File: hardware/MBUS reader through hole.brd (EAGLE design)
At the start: 20.8 x 72.6 mm, 18 parts, among them Q1 BC337, Q2 BC337, T1 BC307

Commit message: modified files
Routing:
- net GND: track 79.1 -> 60.3 mm
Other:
- board text added: "Designed in"
- board text added: "North Wales"
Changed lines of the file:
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@@
 <wire x1="75.7928" y1="7.258" x2="96.4448" y2="7.258" width="0" layer="20"/>
 <wire x1="3" y1="79.9" x2="3" y2="79.4" width="0" layer="121"/>
-<text x="80.914" y="62.7056" size="0.762" layer="121" font="vector" ratio="20" rot="R90">www.openenergymonitor.org</text>
-<text x="82.1692" y="78.1948" size="0.7112" layer="121" font="vector" ratio="20" rot="R270">Designed in North Wales
+<text x="80.914" y="62.7056" size="0.762" layer="21" font="vector" ratio="20" rot="R90">www.openenergymonitor.org</text>
+<text x="82.1692" y="78.1948" size="0.7112" layer="21" font="vector" ratio="20" rot="R270">Designed in North Wales
 by Trystan Lea,
 Glyn Hudson, John Cantor
 and Shiromini Satkunarajah
 </text>
-<text x="81.400640625" y="31.442121875" size="0.7112" layer="21" font="vector" ratio="15" rot="SR0">Made in UK</text>
 <rectangle x1="82.372440625" y1="33.122321875" x2="82.378740625" y2="33.128721875" layer="21"/>
 <rectangle x1="82.366040625" y1="33.128721875" x2="82.378740625" y2="33.135021875" layer="21"/>
@@
 <text x="91.900640625" y="70.742121875" size="0.7112" layer="21" font="vector" ratio="15" rot="SR270">OUT+</text>
 <text x="79.250640625" y="70.192121875" size="0.7112" layer="21" font="vector" ratio="15" rot="SR270">OUT-</text>
+<text x="81.400640625" y="32.342121875" size="0.7112" layer="21" font="vector" ratio="15" rot="SR0">North Wales</text>
+<text x="81.600640625" y="36.942121875" size="0.7112" layer="21" font="vector" ratio="15" rot="SR0">Designed in </text>
+<text x="81.400640625" y="31.292121875" size="0.7112" layer="21" font="vector" ratio="15" rot="SR0">Made in UK</text>
 </plain>
 <attributes>
@@
 <elements>
 <element name="Q1" library="transistor" package="TO92" value="BC337" x="93.1952" y="54.0428" smashed="yes">
-<attribute name="VALUE" x="90.2208" y="52.7304" size="0.8128" layer="27" font="vector" ratio="20" rot="R90"/>
+<attribute name="VALUE" x="90.2208" y="52.7304" size="0.8128" layer="21" font="vector" ratio="20" rot="R90"/>
 </element>
 <element name="Q2" library="transistor" package="TO92" value="BC337" x="93.1952" y="58.5856" smashed="yes">
-<attribute name="VALUE" x="90.2208" y="56.9976" size="0.8128" layer="27" font="vector" ratio="20" rot="R90"/>
+<attribute name="VALUE" x="90.2208" y="56.9976" size="0.8128" layer="21" font="vector" ratio="20" rot="R90"/>
 </element>
 <element name="T1" library="transistor-pnp" package="TO92" value="BC307" x="93.1952" y="64.8904" smashed="yes" rot="R180">
-<attribute name="VALUE" x="90.269" y="63.3796" size="0.8128" layer="27" font="vector" ratio="20" rot="R90"/>
+<attribute name="VALUE" x="90.269" y="63.3796" size="0.8128" layer="21" font="vector" ratio="20" rot="R90"/>
 </element>
 <element name="R3" library="resistor" package="0204/7" value="39k" x="84" y="55" smashed="yes" rot="R180">
 <attribute name="NAME" x="83.3956" y="55.3212" size="0.8128" layer="25" font="vector" ratio="20" rot="R180"/>
-<attribute name="VALUE" x="86.3012" y="55.4736" size="0.8128" layer="27" font="vector" ratio="20" rot="R180"/>
+<attribute name="VALUE" x="86.3012" y="55.4736" size="0.8128" layer="21" font="vector" ratio="20" rot="R180"/>
 </element>
 <element name="R2" library="resistor" package="0204/7" value="33k" x="84.005" y="57.615" smashed="yes" rot="R180">
 <attribute name="NAME" x="83.2456" y="57.862" size="0.8128" layer="25" font="vector" ratio="20" rot="R180"/>
-<attribute name="VALUE" x="86.4488" y="57.9644" size="0.8128" layer="27" font="vector" ratio="20" rot="R180"/>
+<attribute name="VALUE" x="86.4488" y="57.9644" size="0.8128" layer="21" font="vector" ratio="20" rot="R180"/>
 </element>
 <element name="R6" library="resistor" package="0204/7" value="22k" x="82.575" y="45.755" smashed="yes" rot="R90">
@@
 <element name="R1" library="resistor" package="0204/7" value="220k" x="84.005" y="60.155" smashed="yes" rot="R180">
 <attribute name="NAME" x="83.1956" y="60.5028" size="0.8128" layer="25" font="vector" ratio="20" rot="R180"/>
-<attribute name="VALUE" x="86.4012" y="60.4552" size="0.8128" layer="27" font="vector" ratio="20" rot="R180"/>
+<attribute name="VALUE" x="86.4012" y="60.4552" size="0.8128" layer="21" font="vector" ratio="20" rot="R180"/>
 </element>
 <element name="R4" library="resistor" package="0204/7" value="1k" x="84.005" y="52.535" smashed="yes" rot="R180">
 <attribute name="NAME" x="83.2956" y="52.7828" size="0.8128" layer="25" font="vector" ratio="20" rot="R180"/>
-<attribute name="VALUE" x="85.8012" y="52.8828" size="0.8128" layer="27" font="vector" ratio="20" rot="R180"/>
+<attribute name="VALUE" x="85.8012" y="52.8828" size="0.8128" layer="21" font="vector" ratio="20" rot="R180"/>
 </element>
 <element name="R5" library="resistor" package="0204/7" value="1k" x="80.035" y="45.755" smashed="yes" rot="R270">
@@
 <wire x1="94.4652" y1="58.5856" x2="94.4652" y2="60.80113125" width="0.4064" layer="16"/>
 <wire x1="94.4652" y1="60.80113125" x2="93.65813125" y2="61.6082" width="0.4064" layer="16"/>
-<wire x1="86.7934" y1="24.2808" x2="83.8126" y2="21.3" width="0.4064" layer="1"/>
-<wire x1="83.8126" y1="21.3" x2="79.15" y2="21.3" width="0.4064" layer="1"/>
-<wire x1="79.15" y1="21.3" x2="77.5" y2="22.95" width="0.4064" layer="1"/>
-<wire x1="77.5" y1="22.95" x2="77.5" y2="30.5" width="0.4064" layer="1"/>
 </signal>
 <signal name="D5">
@@
 <wire x1="93.1952" y1="60.4906" x2="93.1952" y2="57.4564875" width="0.4064" layer="16"/>
 <wire x1="93.1952" y1="57.4564875" x2="90.8584" y2="55.1196875" width="0.4064" layer="16"/>
-<wire x1="90.8584" y1="55.1196875" x2="90.8584" y2="53.2156" width="0.4064" layer="16"/>
-<wire x1="90.8584" y1="53.2156" x2="87.655" y2="50.0122" width="0.4064" layer="16"/>
+<wire x1="90.8584" y1="55.1196875" x2="90.8584" y2="53.1156" width="0.4064" layer="16"/>
+<wire x1="90.8584" y1="53.1156" x2="87.655" y2="50.0122" width="0.4064" layer="16"/>
 <wire x1="94.4652" y1="64.8904" x2="94.4652" y2="61.7606" width="0.4064" layer="1"/>
 <wire x1="94.4652" y1="61.7606" x2="93.1952" y2="60.4906" width="0.4064" layer="1"/>
@@
 <wire x1="93.1952" y1="55.9478" x2="93.1164" y2="55.869" width="0.4064" layer="1"/>
 <wire x1="93.1164" y1="55.869" x2="93.1164" y2="53.4924" width="0.4064" layer="1"/>
-<wire x1="93.1164" y1="53.4924" x2="92.159" y2="52.535" width="0.4064" layer="1"/>
-<wire x1="92.159" y1="52.535" x2="87.815" y2="52.535" width="0.4064" layer="1"/>
+<wire x1="93.1164" y1="53.4924" x2="91.859" y2="52.535" width="0.4064" layer="1"/>
+<wire x1="91.859" y1="52.535" x2="87.815" y2="52.535" width="0.4064" layer="1"/>
 </signal>
 <signal name="24V">

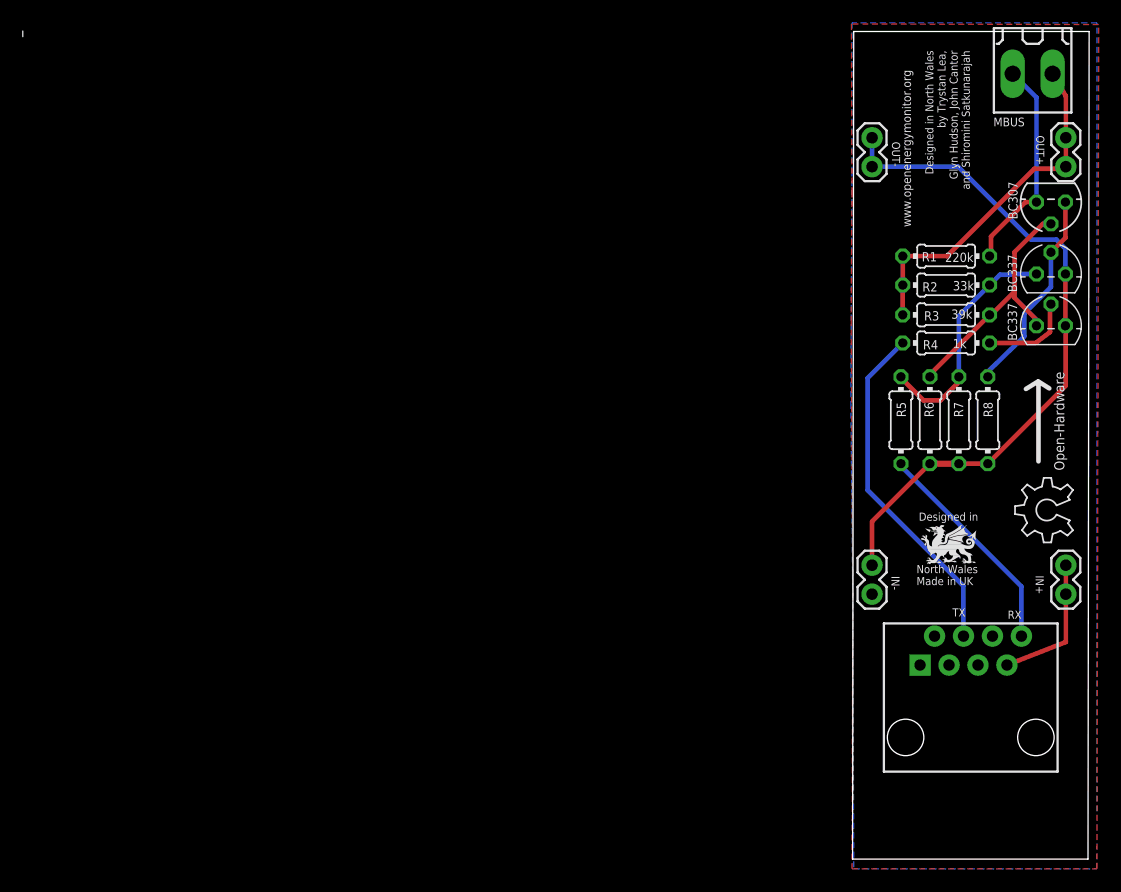
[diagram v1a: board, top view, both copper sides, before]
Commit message: through hole with connector blocks
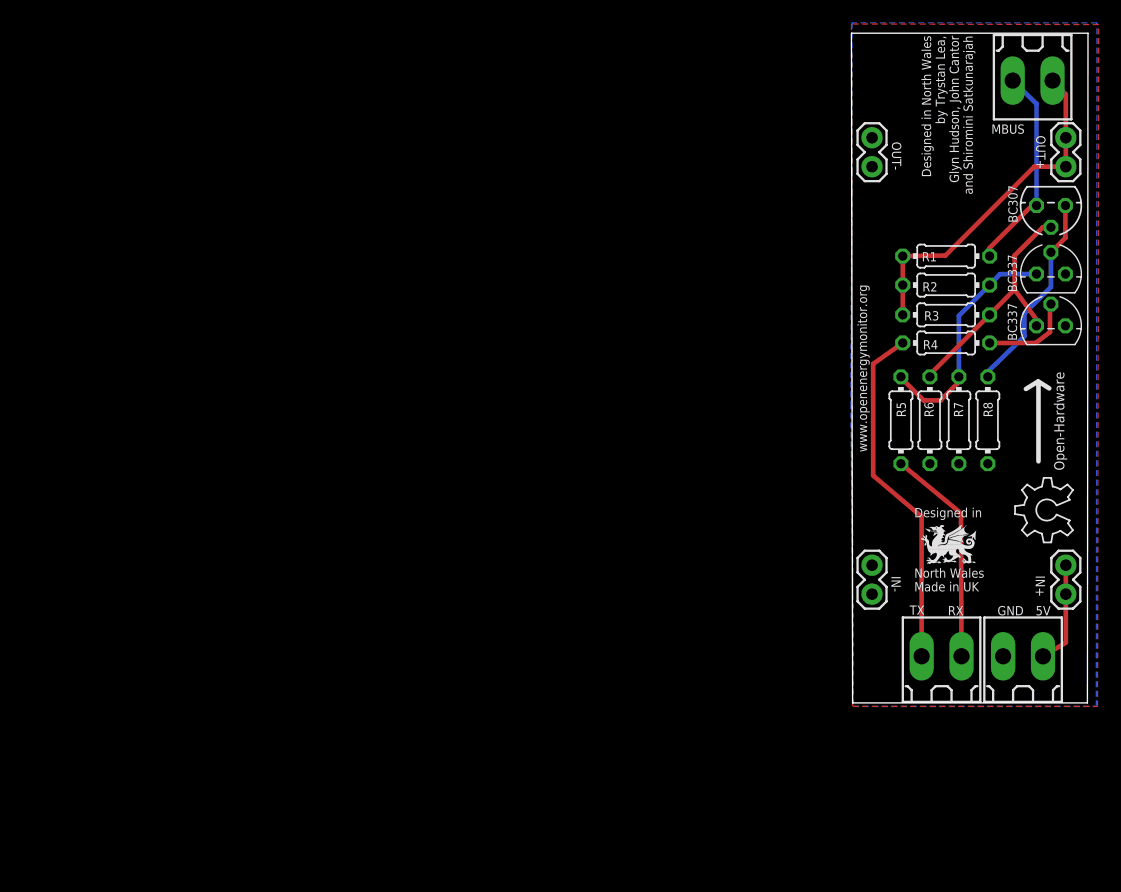
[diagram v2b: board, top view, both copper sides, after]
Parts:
- removed U$13: RJ45-8PTH, SparkFun-Connectors:RJ45-8
- added MBUS1, MBUS2: (no value), con-weidmueller-sl35:180-2
- moved MBUS 0.60 mm to (91.6, 75.6)
- moved T1 0.30 mm to (93.2, 64.6)
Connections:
- net 5V: now also MBUS2.2; no longer U$13.7
- net A6: now also MBUS1.2; no longer U$13.8
- net D5: now also MBUS1.1; no longer U$13.4
- net GND: now also MBUS2.1; no longer U$13.5
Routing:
- net GND: track 60.3 -> 0.04 mm
- net 5V: track 12.3 -> 9.12 mm
- net N$1: track 19.2 -> 18.5 mm
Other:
- board size 20.8 x 72.6 mm -> 20.8 x 58.8 mm
- board text added: "5V"
- board text added: "GND"

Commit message: neater
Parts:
- moved MBUS 5.30 mm to (86.3, 75.6)
- moved MBUS2 1.02 mm to (89.7, 25.1)
- moved MBUS1 1.02 mm to (82.6, 25.1)
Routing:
- net 24V: track 30.7 -> 35.1 mm
- net N$1: track 18.5 -> 20.4 mm
- net A6: track 19.4 -> 18.5 mm
- net 5V: track 9.12 -> 9.94 mm
- net D5: track 31.1 -> 30.3 mm
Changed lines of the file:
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@@
 <setting verticaltext="up"/>
 </settings>
-<grid distance="1.96850394" unitdist="mil" unit="mil" style="lines" multiple="1" display="yes" altdistance="0.635" altunitdist="mm" altunit="mm"/>
+<grid distance="10" unitdist="mil" unit="mil" style="lines" multiple="1" display="yes" altdistance="0.635" altunitdist="mm" altunit="mm"/>
 <layers>
 <layer number="1" name="Top" color="4" fill="1" visible="yes" active="yes"/>
@@
 <wire x1="75.7928" y1="20.958" x2="96.3948" y2="20.958" width="0" layer="20"/>
 <text x="77.064" y="42.9556" size="0.8128" layer="21" font="vector" ratio="20" rot="R90">www.openenergymonitor.org</text>
-<text x="81.8692" y="79.4948" size="0.8128" layer="21" font="vector" ratio="20" rot="R270">Designed in North Wales
+<text x="88.2192" y="60.6988" size="0.8128" layer="21" font="vector" ratio="20" rot="MR270">Designed in North Wales
 by Trystan Lea,
 Glyn Hudson, John Cantor
@@
 </element>
 <element name="LOGO1" library="ohw-logo" package="OSHW_6X200_NOTEXT" value="OSHW_LOGO_6MILX0200-NT" x="95.1238" y="35.0372" rot="R90"/>
-<element name="MBUS" library="con-weidmueller-sl35" library_urn="urn:adsk.eagle:library:199" package="180-2" value="" x="91.5876" y="75.5524" smashed="yes" rot="R180">
-<attribute name="MF" value="" x="91.5876" y="75.5524" size="1.778" layer="27" rot="R180" display="off"/>
-<attribute name="MPN" value="" x="91.5876" y="75.5524" size="1.778" layer="27" rot="R180" display="off"/>
-<attribute name="NAME" x="90.8876" y="71.7024" size="0.8128" layer="25" rot="R180"/>
-<attribute name="OC_FARNELL" value="unknown" x="91.5876" y="75.5524" size="1.778" layer="27" rot="R180" display="off"/>
-<attribute name="OC_NEWARK" value="unknown" x="91.5876" y="75.5524" size="1.778" layer="27" rot="R180" display="off"/>
-<attribute name="VALUE" x="93.3376" y="73.8024" size="1.27" layer="27" rot="R180"/>
+<element name="MBUS" library="con-weidmueller-sl35" library_urn="urn:adsk.eagle:library:199" package="180-2" value="" x="86.2876" y="75.5524" smashed="yes" rot="R180">
+<attribute name="MF" value="" x="86.2876" y="75.5524" size="1.778" layer="27" rot="R180" display="off"/>
+<attribute name="MPN" value="" x="86.2876" y="75.5524" size="1.778" layer="27" rot="R180" display="off"/>
+<attribute name="NAME" x="85.5876" y="71.7024" size="0.8128" layer="25" rot="R180"/>
+<attribute name="OC_FARNELL" value="unknown" x="86.2876" y="75.5524" size="1.778" layer="27" rot="R180" display="off"/>
+<attribute name="OC_NEWARK" value="unknown" x="86.2876" y="75.5524" size="1.778" layer="27" rot="R180" display="off"/>
+<attribute name="VALUE" x="88.0376" y="73.8024" size="1.27" layer="27" rot="R180"/>
 </element>
-<element name="MBUS1" library="con-weidmueller-sl35" library_urn="urn:adsk.eagle:library:199" package="180-2" value="" x="83.6" y="25.05" smashed="yes">
-<attribute name="MF" value="" x="83.6" y="25.05" size="1.778" layer="27" display="off"/>
-<attribute name="MPN" value="" x="83.6" y="25.05" size="1.778" layer="27" display="off"/>
-<attribute name="OC_FARNELL" value="unknown" x="83.6" y="25.05" size="1.778" layer="27" display="off"/>
-<attribute name="OC_NEWARK" value="unknown" x="83.6" y="25.05" size="1.778" layer="27" display="off"/>
-<attribute name="VALUE" x="81.85" y="26.8" size="1.27" layer="27"/>
+<element name="MBUS1" library="con-weidmueller-sl35" library_urn="urn:adsk.eagle:library:199" package="180-2" value="" x="82.584" y="25.05" smashed="yes">
+<attribute name="MF" value="" x="82.584" y="25.05" size="1.778" layer="27" display="off"/>
+<attribute name="MPN" value="" x="82.584" y="25.05" size="1.778" layer="27" display="off"/>
+<attribute name="OC_FARNELL" value="unknown" x="82.584" y="25.05" size="1.778" layer="27" display="off"/>
+<attribute name="OC_NEWARK" value="unknown" x="82.584" y="25.05" size="1.778" layer="27" display="off"/>
+<attribute name="VALUE" x="80.834" y="26.8" size="1.27" layer="27"/>
 </element>
-<element name="MBUS2" library="con-weidmueller-sl35" library_urn="urn:adsk.eagle:library:199" package="180-2" value="" x="90.75" y="25.05" smashed="yes">
-<attribute name="MF" value="" x="90.75" y="25.05" size="1.778" layer="27" display="off"/>
-<attribute name="MPN" value="" x="90.75" y="25.05" size="1.778" layer="27" display="off"/>
-<attribute name="OC_FARNELL" value="unknown" x="90.75" y="25.05" size="1.778" layer="27" display="off"/>
-<attribute name="OC_NEWARK" value="unknown" x="90.75" y="25.05" size="1.778" layer="27" display="off"/>
-<attribute name="VALUE" x="89" y="26.8" size="1.27" layer="27"/>
+<element name="MBUS2" library="con-weidmueller-sl35" library_urn="urn:adsk.eagle:library:199" package="180-2" value="" x="89.734" y="25.05" smashed="yes">
+<attribute name="MF" value="" x="89.734" y="25.05" size="1.778" layer="27" display="off"/>
+<attribute name="MPN" value="" x="89.734" y="25.05" size="1.778" layer="27" display="off"/>
+<attribute name="OC_FARNELL" value="unknown" x="89.734" y="25.05" size="1.778" layer="27" display="off"/>
+<attribute name="OC_NEWARK" value="unknown" x="89.734" y="25.05" size="1.778" layer="27" display="off"/>
+<attribute name="VALUE" x="87.984" y="26.8" size="1.27" layer="27"/>
 </element>
 </elements>
@@
 <wire x1="80.195" y1="52.535" x2="77.6" y2="50.7" width="0.4064" layer="1"/>
 <wire x1="77.6" y1="50.7" x2="77.6" y2="40.9" width="0.4064" layer="1"/>
-<wire x1="77.6" y1="40.9" x2="81.85" y2="37.3" width="0.4064" layer="1"/>
-<wire x1="81.85" y1="37.3" x2="81.85" y2="25.05" width="0.4064" layer="1"/>
+<wire x1="80.58" y1="37.3" x2="77.6" y2="40.9" width="0.4064" layer="1"/>
+<wire x1="80.834" y1="25.05" x2="80.834" y2="37.046" width="0.4064" layer="1"/>
+<wire x1="80.834" y1="37.046" x2="80.58" y2="37.3" width="0.4064" layer="1"/>
 </signal>
 <signal name="5V" class="1">
@@
 <wire x1="94.5" y1="33.04" x2="94.5" y2="30.5" width="0.4064" layer="1"/>
 <contactref element="MBUS2" pad="2"/>
-<wire x1="94.5" y1="30.5" x2="94.5" y2="26.25" width="0.4064" layer="1"/>
-<wire x1="94.5" y1="26.25" x2="92.5" y2="25.05" width="0.4064" layer="1"/>
+<wire x1="94.5" y1="26.399825" x2="94.5" y2="30.5" width="0.4064" layer="1"/>
+<wire x1="94.5" y1="26.399825" x2="94.5" y2="26.25" width="0" layer="19" extent="1-16"/>
+<wire x1="91.484" y1="25.05" x2="94.5" y2="26.399825" width="0.4064" layer="1"/>
 </signal>
 <signal name="N$16">
@@
 <contactref element="R2" pad="2"/>
 <contactref element="JP5" pad="2"/>
-<wire x1="94.5" y1="70.54" x2="94.5" y2="68" width="0.4064" layer="1"/>
+<wire x1="94.5" y1="68" x2="94.5" y2="70.54" width="0.4064" layer="1"/>
 <contactref element="MBUS" pad="1"/>
 <wire x1="80.19" y1="55" x2="80.19" y2="57.61" width="0.4064" layer="1"/>
@@
 <wire x1="80.195" y1="60.155" x2="83.9318" y2="60.205" width="0.4064" layer="1"/>
 <wire x1="91.7268" y1="68" x2="83.9318" y2="60.205" width="0.4064" layer="1"/>
-<wire x1="94.5" y1="70.54" x2="94.5" y2="74.35" width="0.4064" layer="1"/>
-<wire x1="94.5" y1="74.35" x2="93.3376" y2="75.5524" width="0.4064" layer="1"/>
 <wire x1="94.5" y1="68" x2="91.7268" y2="68" width="0.4064" layer="1"/>
+<wire x1="88.0236" y1="73.2664" x2="88.0376" y2="75.5524" width="0.4064" layer="1"/>
+<wire x1="94.5" y1="70.54" x2="91.004" y2="70.54" width="0.4064" layer="1"/>
+<wire x1="91.004" y1="70.54" x2="88.0236" y2="73.2664" width="0.4064" layer="1"/>
 </signal>
 <signal name="N$30">
@@
 <contactref element="T1" pad="1"/>
 <contactref element="R1" pad="1"/>
-<wire x1="91.9366" y1="64.9018" x2="91.9252" y2="64.5904" width="0.4064" layer="16"/>
-<wire x1="91.9252" y1="64.5904" x2="91.9252" y2="73.5148" width="0.4064" layer="16"/>
-<wire x1="91.9252" y1="73.5148" x2="89.8376" y2="75.5524" width="0.4064" layer="16"/>
 <wire x1="87.815" y1="60.8802" x2="87.815" y2="60.155" width="0.4064" layer="1"/>
-<wire x1="91.9252" y1="64.5904" x2="91.5252" y2="64.5904" width="0.4064" layer="1"/>
+<wire x1="91.5252" y1="64.5904" x2="91.9252" y2="64.5904" width="0.4064" layer="1"/>
 <wire x1="91.5252" y1="64.5904" x2="87.815" y2="60.8802" width="0.4064" layer="1"/>
+<wire x1="84.5376" y1="75.5524" x2="84.5376" y2="73.7044" width="0.4064" layer="16"/>
+<wire x1="84.5376" y1="73.7044" x2="91.948" y2="66.294" width="0.4064" layer="16"/>
+<wire x1="91.948" y1="66.294" x2="91.948" y2="64.6132" width="0.4064" layer="16"/>
+<wire x1="91.948" y1="64.6132" x2="91.9252" y2="64.5904" width="0.4064" layer="16"/>
 </signal>
 <signal name="A6">
 <contactref element="R5" pad="2"/>
 <contactref element="MBUS1" pad="2"/>
-<wire x1="80.035" y1="41.945" x2="85.3" y2="37.6" width="0.4064" layer="1"/>
-<wire x1="85.3" y1="37.6" x2="85.35" y2="25.05" width="0.4064" layer="1"/>
+<wire x1="84.334" y1="37.050696875" x2="84.334" y2="25.05" width="0.4064" layer="1"/>
+<wire x1="80.035" y1="41.945" x2="84.334" y2="37.050696875" width="0.4064" layer="1"/>
 </signal>
 </signals>
